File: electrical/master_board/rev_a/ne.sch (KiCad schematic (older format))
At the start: 23 parts

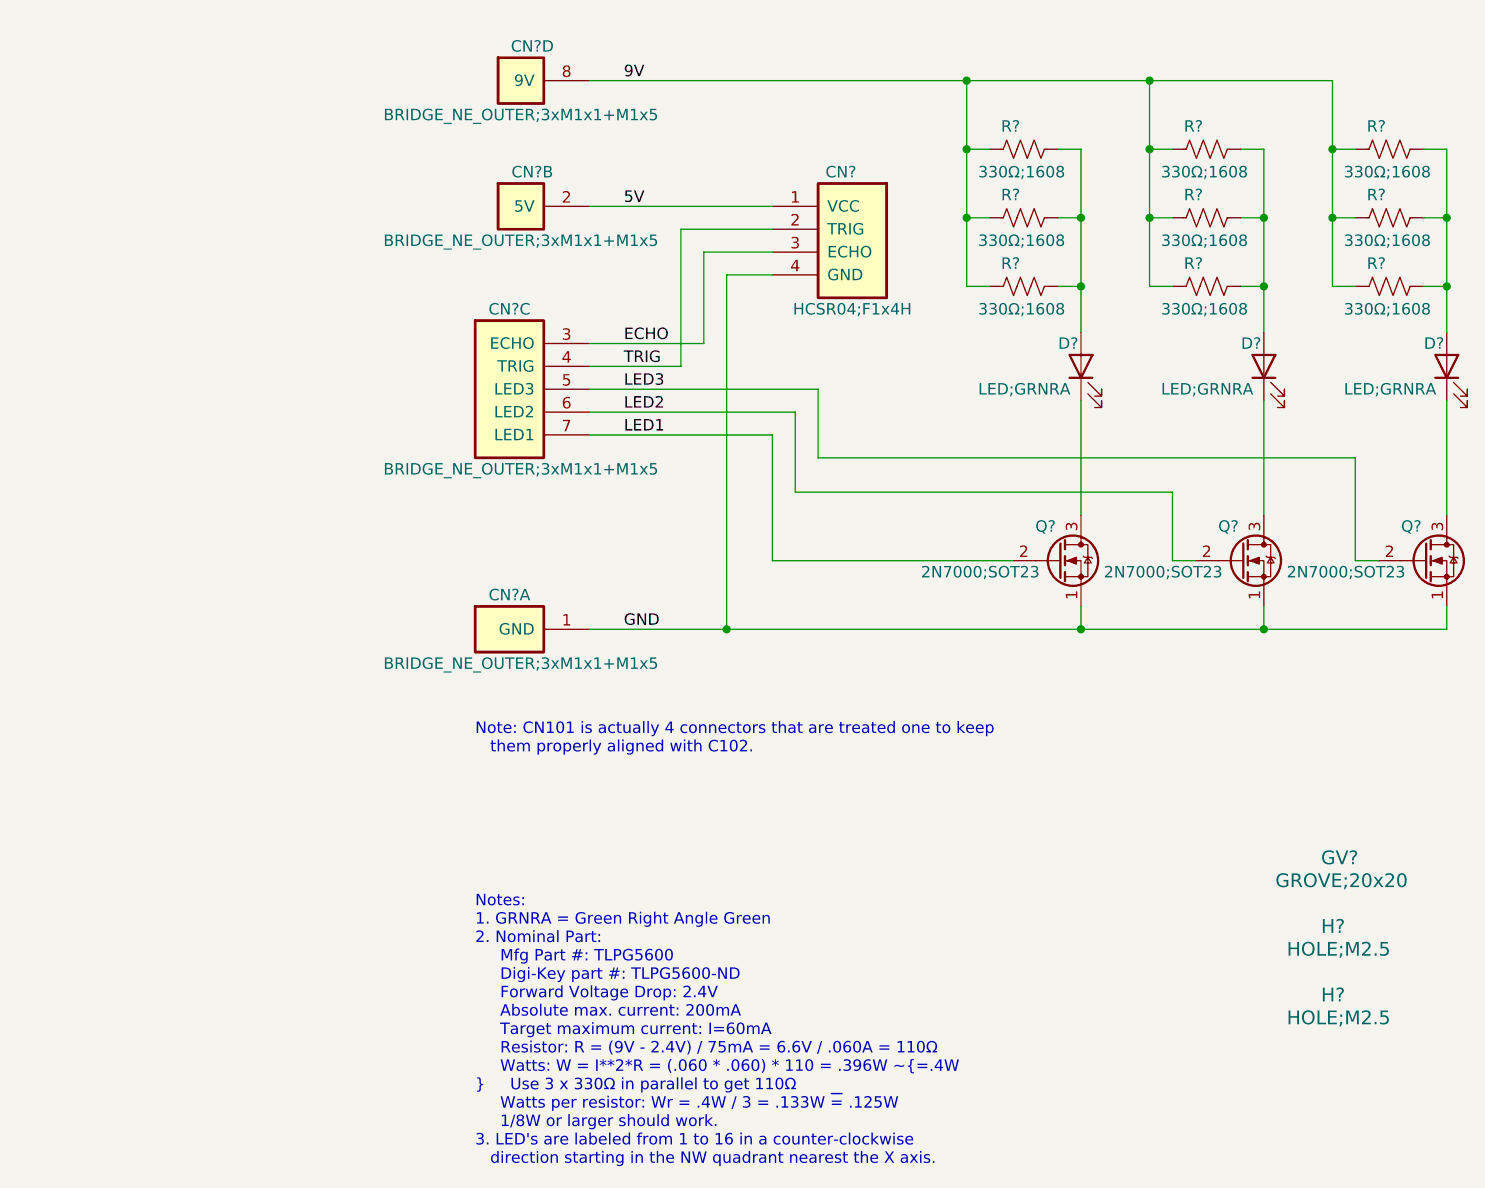
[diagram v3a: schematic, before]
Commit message: Reworked Sonars, Servers, and LED's schematics.
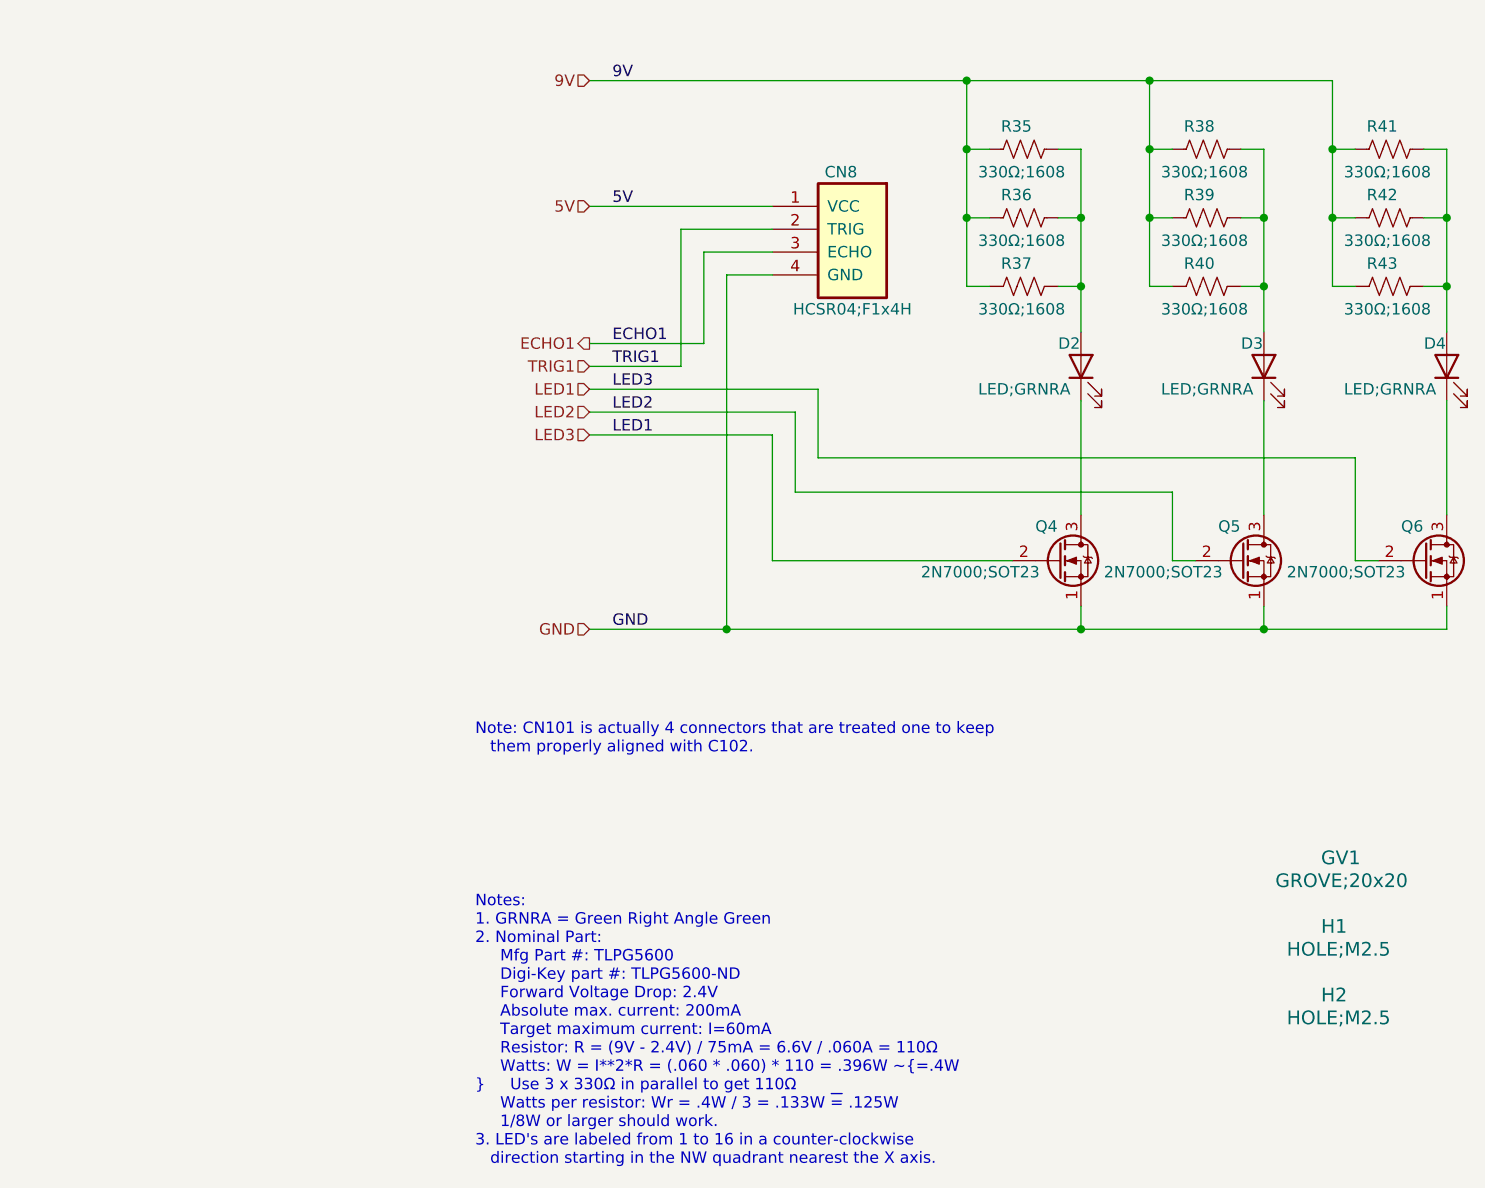
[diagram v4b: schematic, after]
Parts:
- removed CN? (x4): BRIDGE_NE_OUTER;3xM1x1+M1x5, HR2:BRIDGE_NE_OUTER_3xM1x1+M1x5, symbol HR2:BRIDGE_NE_OUTER;3xM1x1+M1x5
- gave numbers to parts that had none: 19
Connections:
- net LED3 is gone; now on net LED1: Q6.2 (G)
- net ECHO renamed ECHO1
- net TRIG renamed TRIG1
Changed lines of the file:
@@
 $Descr A 11000 8500
 encoding utf-8
-Sheet 9 12
-Title "HR2 NE PCB"
-Date "2020-06-13"
+Sheet 12 11
+Title "HR2 Master Board"
+Date "2020-10-03"
 Rev "A"
-Comp "Homebrew Robotics Club"
-Comment1 ""
-Comment2 ""
+Comp "HomeBrew Robotics Club"
+Comment1 "Copyright © 2020 by HomeBrew Robotics Club "
+Comment2 "MIT License"
 Comment3 ""
 Comment4 ""
 $EndDescr
 $Comp
-L HR2:HCSR04H;F1X4 CN?
+L HR2:HCSR04H;F1X4 CN8
 U 1 1 5EE6BF38
 P 5500 1600
-F 0 "CN?" H 5900 1750 50  0000 C CNN
+F 0 "CN8" H 5900 1750 50  0000 C CNN
 F 1 "HCSR04;F1x4H" H 5850 1150 50  0000 C CNN
 F 2 "HR2:HCSR04_F1x4H" H 5700 1650 60  0001 L CNN
@@
 $EndComp
 $Comp
-L HR2:HOLE;M2.5 H?
+L HR2:HOLE;M2.5 H2
 U 1 1 5F2F7E7C
 P 7300 5100
-F 0 "H?" H 7200 5150 60  0000 L CNN
+F 0 "H2" H 7200 5150 60  0000 L CNN
 F 1 "HOLE;M2.5" H 7050 5050 60  0000 L CNN
 F 2 "MountingHole:MountingHole_2.7mm_M2.5" H 7500 5150 60  0001 L CNN
@@
 $EndComp
 $Comp
-L HR2:HOLE;M2.5 H?
+L HR2:HOLE;M2.5 H1
 U 1 1 5F2F85AA
 P 7300 4800
-F 0 "H?" H 7200 4850 60  0000 L CNN
+F 0 "H1" H 7200 4850 60  0000 L CNN
 F 1 "HOLE;M2.5" H 7050 4750 60  0000 L CNN
 F 2 "MountingHole:MountingHole_2.7mm_M2.5" H 7500 4850 60  0001 L CNN
@@
 $EndComp
 $Comp
-L HR2:GROVE;20x20 GV?
+L HR2:GROVE;20x20 GV1
 U 1 1 5F2F9731
 P 7300 4500
-F 0 "GV?" H 7200 4550 60  0000 L CNN
+F 0 "GV1" H 7200 4550 60  0000 L CNN
 F 1 "GROVE;20x20" H 7000 4450 60  0000 L CNN
 F 2 "HR2:GROVE20x20" H 7500 4550 60  0001 L CNN
@@
 $EndComp
 $Comp
-L Device:LED D?
+L Device:LED D2
 U 1 1 5F30B259
 P 6150 2300
-F 0 "D?" V 6250 2400 50  0000 R CNN
+F 0 "D2" V 6250 2400 50  0000 R CNN
 F 1 "LED;GRNRA" V 6050 2750 50  0000 R CNN
 F 2 "HR2:LED_GRNRA" H 6150 2300 50  0001 C CNN
@@
 	0    -1   -1   0
 $EndComp
-Text Label 4150 3450 0    50   ~ 0
+Text Label 4100 3450 0    50   ~ 0
 GND
 $Comp
-L Transistor_FET:2N7000 Q?
+L Transistor_FET:2N7000 Q4
 U 1 1 5F4294E7
 P 6050 3150
-F 0 "Q?" H 5950 3300 50  0000 L CNN
+F 0 "Q4" H 5950 3300 50  0000 L CNN
 F 1 "2N7000;SOT23" H 5450 3100 50  0000 L CNN
 F 2 "Package_TO_SOT_SMD:SOT-23" H 6250 3075 50  0001 L CIN
@@
 $EndComp
 $Comp
-L Device:R_US R?
+L Device:R_US R43
 U 1 1 5F429CFC
 P 7500 1950
-F 0 "R?" V 7400 1850 50  0000 L CNN
+F 0 "R43" V 7400 1850 50  0000 L CNN
 F 1 "330Ω;1608" V 7600 1750 50  0000 L CNN
 F 2 "Resistor_SMD:R_0603_1608Metric" V 7540 1940 50  0001 C CNN
@@
 Notes:\n1. GRNRA = Green Right Angle Green\n2. Nominal Part:\n     Mfg Part #: TLPG5600\n     Digi-Key part #: TLPG5600-ND\n     Forward Voltage Drop: 2.4V\n     Absolute max. current: 200mA\n     Target maximum current: I=60mA\n     Resistor: R = (9V - 2.4V) / 75mA = 6.6V / .060A = 110Ω\n     Watts: W = I**2*R = (.060 * .060) * 110 = .396W ~=.4W\n     Use 3 x 330Ω in parallel to get 110Ω\n     Watts per resistor: Wr = .4W / 3 = .133W ~= .125W\n     1/8W or larger should work.\n3. LED's are labeled from 1 to 16 in a counter-clockwise\n   direction starting in the NW quadrant nearest the X axis.
 $Comp
-L Device:R_US R?
+L Device:R_US R42
 U 1 1 5F42F445
 P 7500 1650
-F 0 "R?" V 7400 1550 50  0000 L CNN
+F 0 "R42" V 7400 1550 50  0000 L CNN
 F 1 "330Ω;1608" V 7600 1450 50  0000 L CNN
 F 2 "Resistor_SMD:R_0603_1608Metric" V 7540 1640 50  0001 C CNN
@@
 $EndComp
 $Comp
-L Device:R_US R?
+L Device:R_US R41
 U 1 1 5F42F75B
 P 7500 1350
-F 0 "R?" V 7400 1250 50  0000 L CNN
+F 0 "R41" V 7400 1250 50  0000 L CNN
 F 1 "330Ω;1608" V 7600 1150 50  0000 L CNN
 F 2 "Resistor_SMD:R_0603_1608Metric" V 7540 1340 50  0001 C CNN
@@
 	6150 2950 6150 2450
 $Comp
-L Device:LED D?
+L Device:LED D3
 U 1 1 5F436F00
 P 6950 2300
-F 0 "D?" V 7050 2400 50  0000 R CNN
+F 0 "D3" V 7050 2400 50  0000 R CNN
 F 1 "LED;GRNRA" V 6850 2750 50  0000 R CNN
 F 2 "HR2:LED_GRNRA" H 6950 2300 50  0001 C CNN
@@
 $EndComp
 $Comp
-L Transistor_FET:2N7000 Q?
+L Transistor_FET:2N7000 Q5
 U 1 1 5F436F0A
 P 6850 3150
-F 0 "Q?" H 6750 3300 50  0000 L CNN
+F 0 "Q5" H 6750 3300 50  0000 L CNN
 F 1 "2N7000;SOT23" H 6250 3100 50  0000 L CNN
 F 2 "Package_TO_SOT_SMD:SOT-23" H 7050 3075 50  0001 L CIN
@@
 $EndComp
 $Comp
-L Device:R_US R?
+L Device:R_US R40
 U 1 1 5F436F14
 P 6700 1950
-F 0 "R?" V 6600 1850 50  0000 L CNN
+F 0 "R40" V 6600 1850 50  0000 L CNN
 F 1 "330Ω;1608" V 6800 1750 50  0000 L CNN
 F 2 "Resistor_SMD:R_0603_1608Metric" V 6740 1940 50  0001 C CNN
@@
 $EndComp
 $Comp
-L Device:R_US R?
+L Device:R_US R39
 U 1 1 5F436F1E
 P 6700 1650
-F 0 "R?" V 6600 1550 50  0000 L CNN
+F 0 "R39" V 6600 1550 50  0000 L CNN
 F 1 "330Ω;1608" V 6800 1450 50  0000 L CNN
 F 2 "Resistor_SMD:R_0603_1608Metric" V 6740 1640 50  0001 C CNN
@@
 $EndComp
 $Comp
-L Device:R_US R?
+L Device:R_US R38
 U 1 1 5F436F28
 P 6700 1350
-F 0 "R?" V 6600 1250 50  0000 L CNN
+F 0 "R38" V 6600 1250 50  0000 L CNN
 F 1 "330Ω;1608" V 6800 1150 50  0000 L CNN
 F 2 "Resistor_SMD:R_0603_1608Metric" V 6740 1340 50  0001 C CNN
@@
 Connection ~ 6450 1350
 $Comp
-L Device:LED D?
+L Device:LED D4
 U 1 1 5F43BB9D
 P 7750 2300
-F 0 "D?" V 7850 2400 50  0000 R CNN
+F 0 "D4" V 7850 2400 50  0000 R CNN
 F 1 "LED;GRNRA" V 7650 2750 50  0000 R CNN
 F 2 "HR2:LED_GRNRA" H 7750 2300 50  0001 C CNN
@@
 $EndComp
 $Comp
-L Device:R_US R?
+L Device:R_US R37
 U 1 1 5F43BBB1
 P 5900 1950
-F 0 "R?" V 5800 1850 50  0000 L CNN
+F 0 "R37" V 5800 1850 50  0000 L CNN
 F 1 "330Ω;1608" V 6000 1750 50  0000 L CNN
 F 2 "Resistor_SMD:R_0603_1608Metric" V 5940 1940 50  0001 C CNN
@@
 $EndComp
 $Comp
-L Device:R_US R?
+L Device:R_US R36
 U 1 1 5F43BBBB
 P 5900 1650
-F 0 "R?" V 5800 1550 50  0000 L CNN
+F 0 "R36" V 5800 1550 50  0000 L CNN
 F 1 "330Ω;1608" V 6000 1450 50  0000 L CNN
 F 2 "Resistor_SMD:R_0603_1608Metric" V 5940 1640 50  0001 C CNN
@@
 $EndComp
 $Comp
-L Device:R_US R?
+L Device:R_US R35
 U 1 1 5F43BBC5
 P 5900 1350
-F 0 "R?" V 5800 1250 50  0000 L CNN
+F 0 "R35" V 5800 1250 50  0000 L CNN
 F 1 "330Ω;1608" V 6000 1150 50  0000 L CNN
 F 2 "Resistor_SMD:R_0603_1608Metric" V 5940 1340 50  0001 C CNN
@@
 	4000 1600 4800 1600
 $Comp
-L Transistor_FET:2N7000 Q?
+L Transistor_FET:2N7000 Q6
 U 1 1 5F43BBA7
 P 7650 3150
-F 0 "Q?" H 7550 3300 50  0000 L CNN
+F 0 "Q6" H 7550 3300 50  0000 L CNN
 F 1 "2N7000;SOT23" H 7050 3100 50  0000 L CNN
 F 2 "Package_TO_SOT_SMD:SOT-23" H 7850 3075 50  0001 L CIN
@@
 Wire Wire Line
 	5000 2400 4000 2400
+Text Label 4100 2400 0    50   ~ 0
+LED3
+Text Label 4100 2500 0    50   ~ 0
+LED2
+Text Label 4100 2600 0    50   ~ 0
+LED1
+Text Label 4100 2300 0    50   ~ 0
+TRIG1
+Text Label 4100 2200 0    50   ~ 0
+ECHO1
+Text Label 4100 1600 0    50   ~ 0
+5V
+Text Label 4100 1050 0    50   ~ 0
+9V
 Text Notes 3500 4000 0    50   ~ 0
 Note: CN101 is actually 4 connectors that are treated one to keep\n   them properly aligned with C102.
-$Comp
-L HR2:BRIDGE_NE_OUTER;3xM1x1+M1x5 CN?
-U 1 1 5F442084
-P 3300 3450
-F 0 "CN?" H 3650 3600 50  0000 C CNN
-F 1 "BRIDGE_NE_OUTER;3xM1x1+M1x5" H 3700 3300 50  0000 C CNN
-F 2 "HR2:BRIDGE_NE_OUTER_3xM1x1+M1x5" H 3500 3500 60  0001 L CNN
-F 3 "" H 3500 3300 60  0001 L CNN
-F 4 "NE Outer Bridge Connectors" H 3500 3200 60  0001 L CNN "Field5"
-	1    3300 3450
-	1    0    0    -1
-$EndComp
-$Comp
-L HR2:BRIDGE_NE_OUTER;3xM1x1+M1x5 CN?
-U 2 1 5F44303C
-P 3400 1600
-F 0 "CN?" H 3750 1750 50  0000 C CNN
-F 1 "BRIDGE_NE_OUTER;3xM1x1+M1x5" H 3700 1450 50  0000 C CNN
-F 2 "HR2:BRIDGE_NE_OUTER_3xM1x1+M1x5" H 3600 1650 60  0001 L CNN
-F 3 "" H 3600 1450 60  0001 L CNN
-F 4 "NE Outer Bridge Connectors" H 3600 1350 60  0001 L CNN "Field5"
-	2    3400 1600
-	1    0    0    -1
-$EndComp
-$Comp
-L HR2:BRIDGE_NE_OUTER;3xM1x1+M1x5 CN?
-U 4 1 5F44482A
-P 3400 1050
-F 0 "CN?" H 3750 1200 50  0000 C CNN
-F 1 "BRIDGE_NE_OUTER;3xM1x1+M1x5" H 3700 900 50  0000 C CNN
-F 2 "HR2:BRIDGE_NE_OUTER_3xM1x1+M1x5" H 3600 1100 60  0001 L CNN
-F 3 "" H 3600 900 60  0001 L CNN
-F 4 "NE Outer Bridge Connectors" H 3600 800 60  0001 L CNN "Field5"
-	4    3400 1050
-	1    0    0    -1
-$EndComp
-$Comp
-L HR2:BRIDGE_NE_OUTER;3xM1x1+M1x5 CN?
-U 3 1 5F445670
-P 3300 2200
-F 0 "CN?" H 3650 2350 50  0000 C CNN
-F 1 "BRIDGE_NE_OUTER;3xM1x1+M1x5" H 3700 1650 50  0000 C CNN
-F 2 "HR2:BRIDGE_NE_OUTER_3xM1x1+M1x5" H 3500 2250 60  0001 L CNN
-F 3 "" H 3500 2050 60  0001 L CNN
-F 4 "NE Outer Bridge Connectors" H 3500 1950 60  0001 L CNN "Field5"
-	3    3300 2200
-	1    0    0    -1
-$EndComp
-Text Label 4150 2400 0    50   ~ 0
+Text HLabel 4000 1050 0    50   Input ~ 0
+9V
+Text HLabel 4000 1600 0    50   Input ~ 0
+5V
+Text HLabel 4000 3450 0    50   Input ~ 0
+GND
+Text HLabel 4000 2300 0    50   Input ~ 0
+TRIG1
+Text HLabel 4000 2400 0    50   Input ~ 0
+LED1
+Text HLabel 4000 2500 0    50   Input ~ 0
+LED2
+Text HLabel 4000 2600 0    50   Input ~ 0
 LED3
-Text Label 4150 2500 0    50   ~ 0
-LED2
-Text Label 4150 2600 0    50   ~ 0
-LED1
-Text Label 4150 2300 0    50   ~ 0
-TRIG
-Text Label 4150 2200 0    50   ~ 0
-ECHO
-Text Label 4150 1600 0    50   ~ 0
-5V
-Text Label 4150 1050 0    50   ~ 0
-9V
+Text HLabel 4000 2200 0    50   Output ~ 0
+ECHO1
 $EndSCHEMATC
